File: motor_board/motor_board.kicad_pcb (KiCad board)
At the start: 4 copper layers, 47.9 x 29.7 mm, 30 parts, among them J1 Conn_01x05_Female, J3 Conn_01x06_Male, J4 Conn_01x06_Male, J7 Conn_01x06_Male, J8 Conn_01x06_Male, SW1 SW_Push, U1 ATmega32U4-A, U2 DRV8833PW, U4 DRV8833PW, Y1 Crystal_GND24

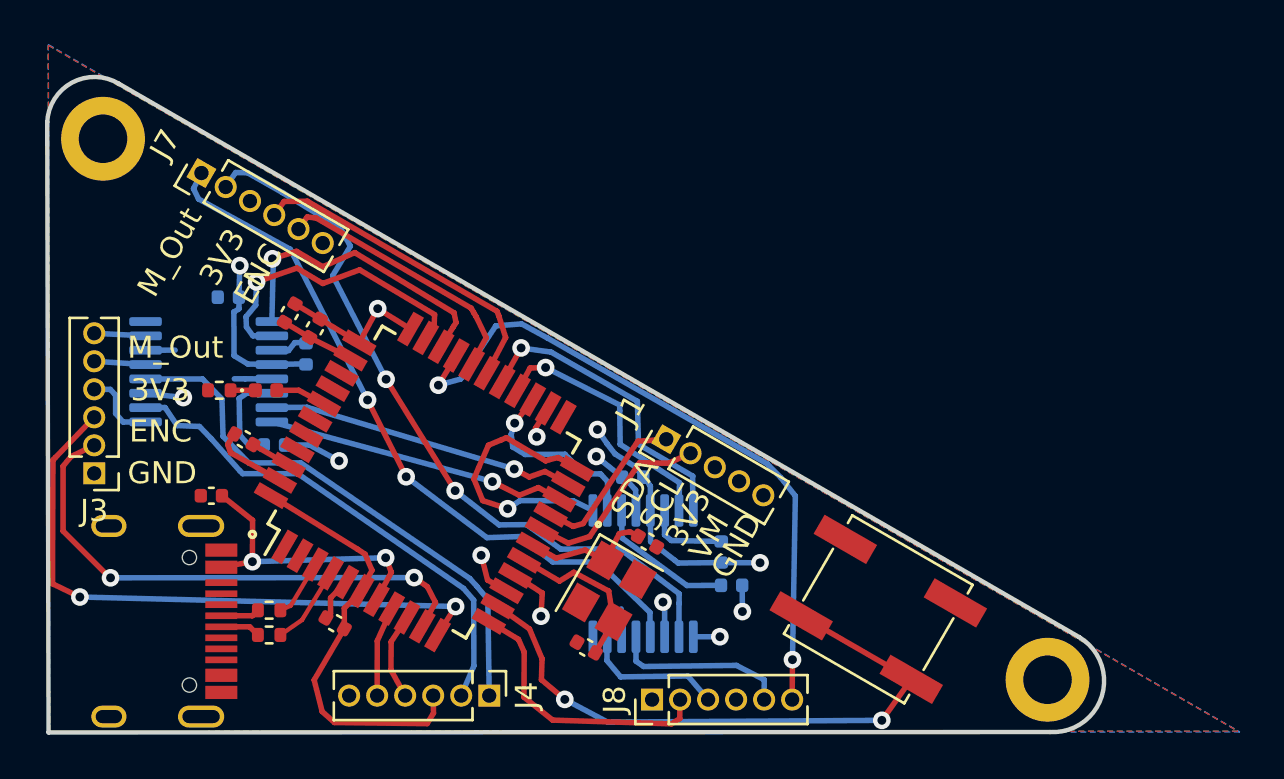
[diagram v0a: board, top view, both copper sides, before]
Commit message: Fixed multipled pours on same plane
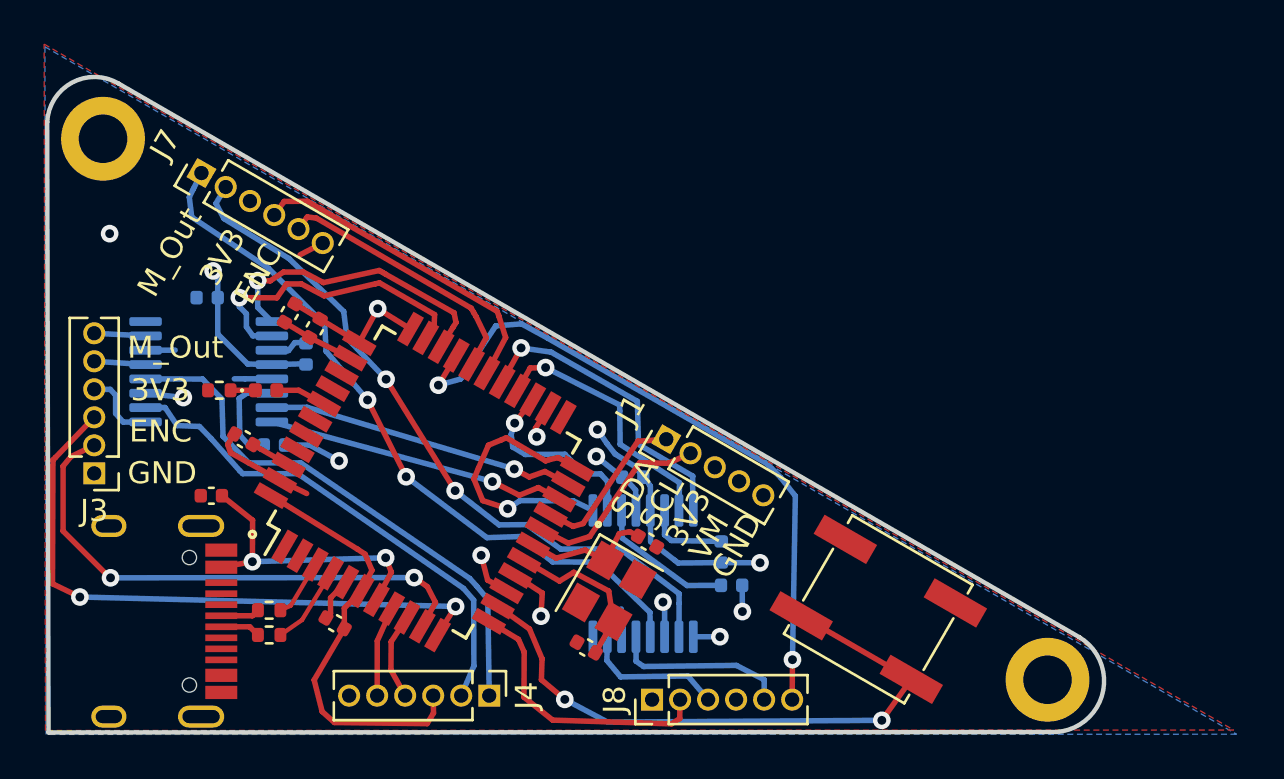
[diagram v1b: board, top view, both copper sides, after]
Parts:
- moved C9 0.96 mm to (45.9, 86.1)
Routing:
- net GND: track 33.1 -> 35.7 mm, vias 6 -> 7
- net Net-(J7-Pad2): track 33.6 -> 32.0 mm
- removed copper zone on In1.Cu, net GND
- removed copper zone on In2.Cu, net GND

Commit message: Recent JLC order for motor controllers
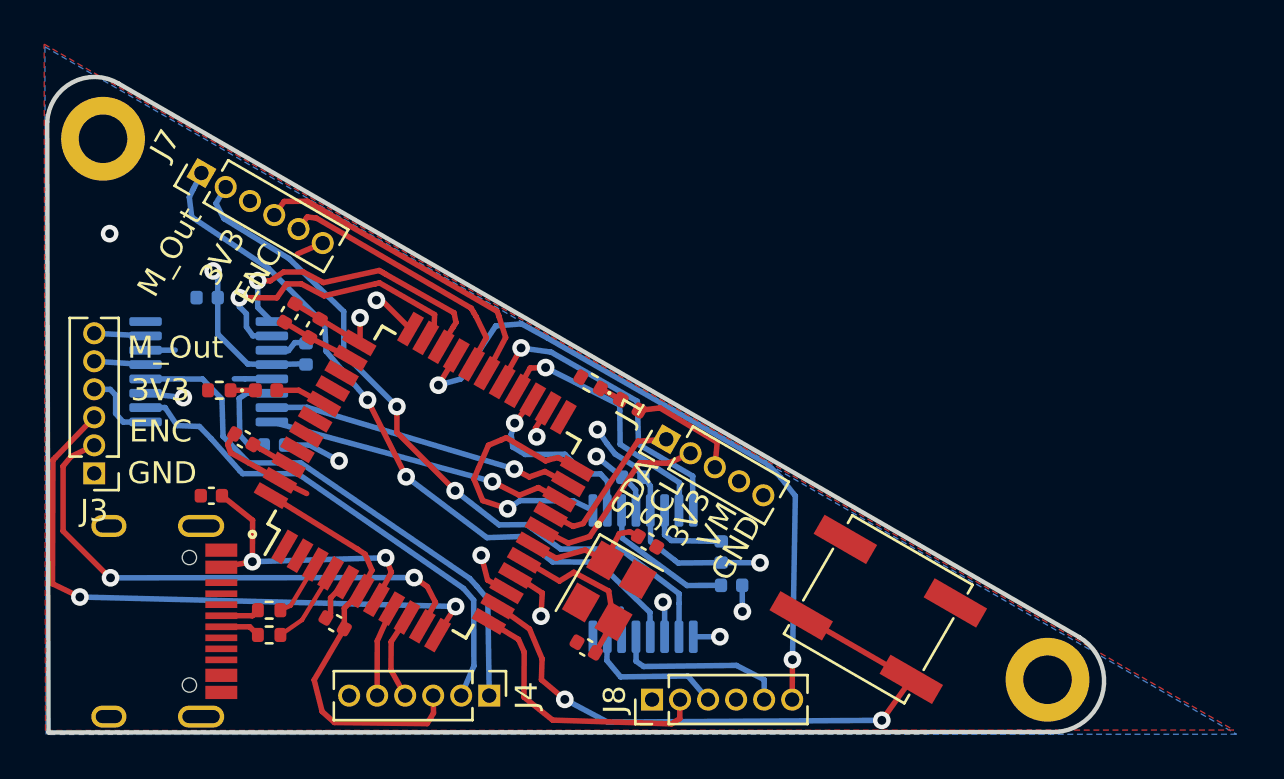
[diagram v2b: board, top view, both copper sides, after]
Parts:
- added D2: LED, LED_SMD:LED_0402_1005Metric, F.Cu at (65.1, 90.9)
- added R4: 220, Resistor_SMD:R_0402_1005Metric, F.Cu at (63.3, 89.9)
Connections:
- U1 pad 33: +3V3 -> GND
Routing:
- net +3V3: track 37.6 -> 40.3 mm
- net GND: track 35.7 -> 37.8 mm, vias 7 -> 8
- net Net-(D2-Pad1): track 0.00 -> 1.06 mm
